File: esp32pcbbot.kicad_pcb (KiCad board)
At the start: 2 copper layers, 110 x 170 mm, 44 parts, among them IC1 BMI055, J1 TB002-500-02BE, J2 TB002-500-02BE, J3 TB002-500-02BE, J4 215299-4, J5 SSQ-120-01-L-D, J6 215299-4, Q1 2N7002, Q2 2N7002, Q3 Q_Photo_NPN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

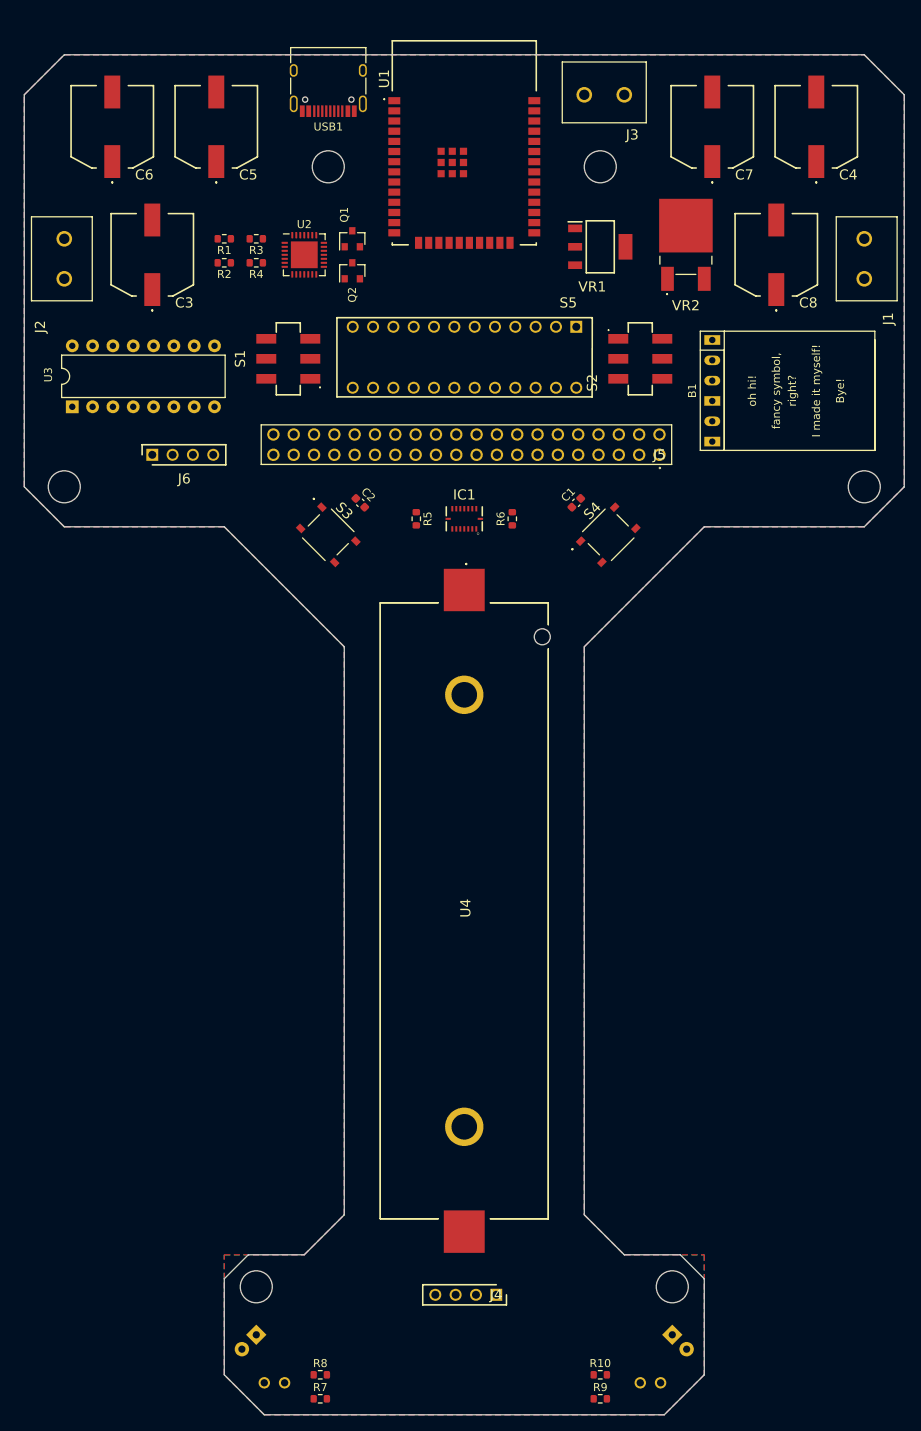
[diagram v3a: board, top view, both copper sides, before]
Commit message: rearranged AGAIN for auto routing
wow this is getting really annoying. I hope it works this time.
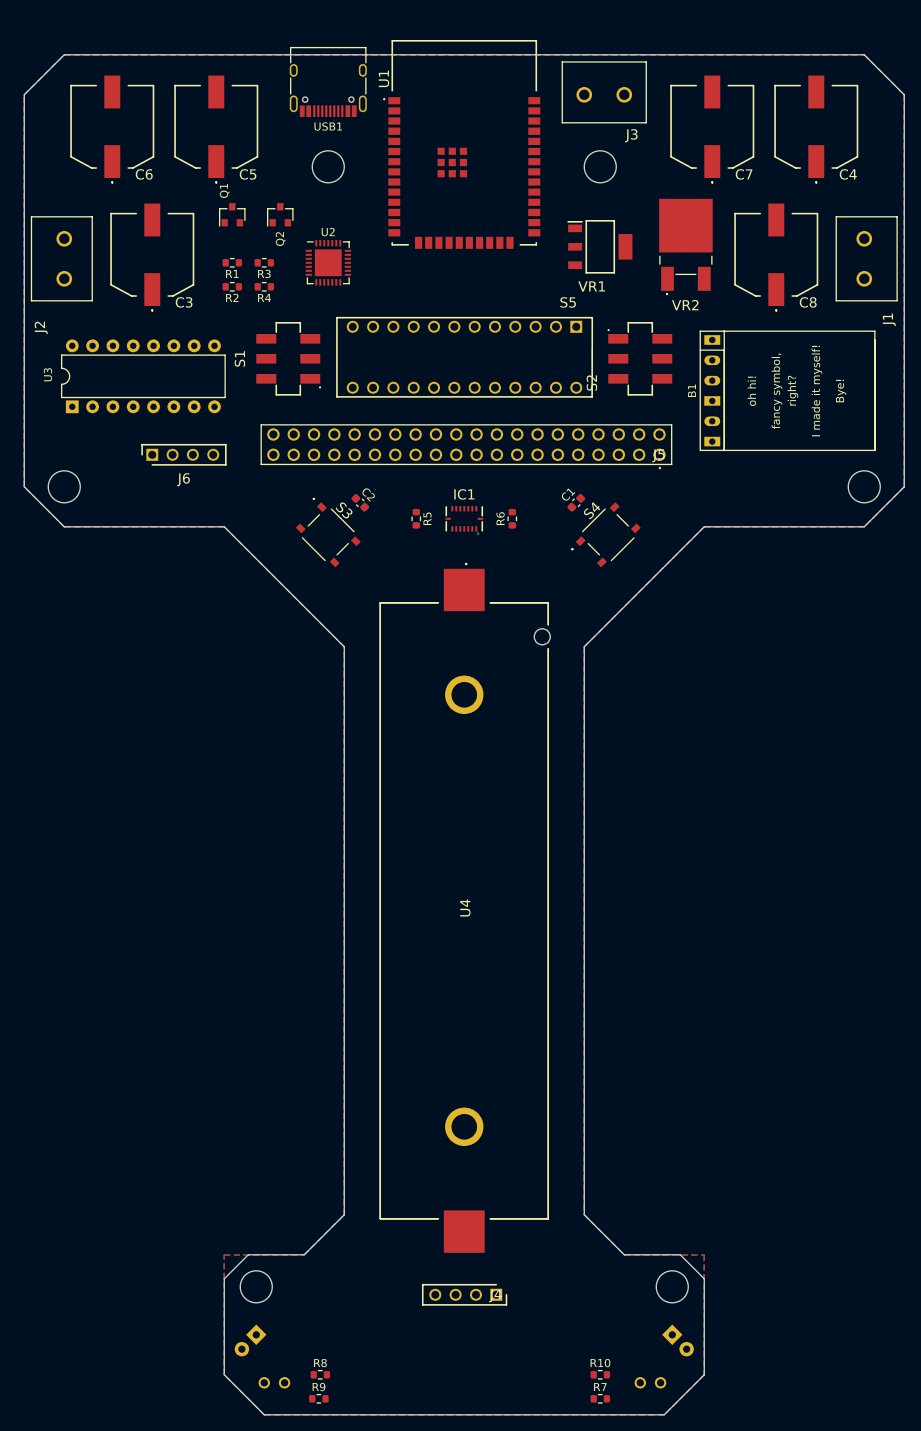
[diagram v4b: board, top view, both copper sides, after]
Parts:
- moved R9 35.2 mm to (71.8, 193.0)
- moved R7 35.0 mm to (107.0, 193.0)
- moved Q1 15.3 mm to (61.0, 45.0)
- moved Q2 11.4 mm to (67.0, 45.0)
- moved R1 3.16 mm to (61.0, 51.0)
- moved R2 3.16 mm to (61.0, 54.0)
- moved R3 3.16 mm to (65.0, 51.0)
- moved R4 3.16 mm to (65.0, 54.0)
- moved U2 3.16 mm to (73.0, 51.0)
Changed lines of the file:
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@@
   )
   (module Package_DFN_QFN:QFN-28-1EP_5x5mm_P0.5mm_EP3.35x3.35mm (layer F.Cu)
-    (at 70 50)
+    (at 73 51)
     (descr "QFN, 28 Pin (http://ww1.microchip.com/downloads/en/PackagingSpec/00000049BQ.pdf#page=283), generated with kicad-footprint-generator ipc_noLead_generator.py")
     (tags "QFN NoLead")
@@
   )
   (module Resistor_SMD:R_0603_1608Metric (layer F.Cu)
-    (at 107 193)
+    (at 71.825 193)
     (descr "Resistor SMD 0603 (1608 Metric), square (rectangular) end terminal, IPC_7351 nominal, (Body size source: IPC-SM-782 page 72, https://www.pcb-3d.com/wordpress/wp-content/uploads/ipc-sm-782a_amendment_1_and_2.pdf), generated with kicad-footprint-generator")
     (tags resistor)
@@
   )
   (module Resistor_SMD:R_0603_1608Metric (layer F.Cu)
-    (at 72 193)
+    (at 107 193)
     (descr "Resistor SMD 0603 (1608 Metric), square (rectangular) end terminal, IPC_7351 nominal, (Body size source: IPC-SM-782 page 72, https://www.pcb-3d.com/wordpress/wp-content/uploads/ipc-sm-782a_amendment_1_and_2.pdf), generated with kicad-footprint-generator")
     (tags resistor)
@@
   )
   (module Resistor_SMD:R_0603_1608Metric (layer F.Cu)
-    (at 64 51 180)
+    (at 65 54 180)
     (descr "Resistor SMD 0603 (1608 Metric), square (rectangular) end terminal, IPC_7351 nominal, (Body size source: IPC-SM-782 page 72, https://www.pcb-3d.com/wordpress/wp-content/uploads/ipc-sm-782a_amendment_1_and_2.pdf), generated with kicad-footprint-generator")
     (tags resistor)
@@
   )
   (module Resistor_SMD:R_0603_1608Metric (layer F.Cu)
-    (at 64 48 180)
+    (at 65 51 180)
     (descr "Resistor SMD 0603 (1608 Metric), square (rectangular) end terminal, IPC_7351 nominal, (Body size source: IPC-SM-782 page 72, https://www.pcb-3d.com/wordpress/wp-content/uploads/ipc-sm-782a_amendment_1_and_2.pdf), generated with kicad-footprint-generator")
     (tags resistor)
@@
   )
   (module Resistor_SMD:R_0603_1608Metric (layer F.Cu)
-    (at 60 51 180)
+    (at 61 54 180)
     (descr "Resistor SMD 0603 (1608 Metric), square (rectangular) end terminal, IPC_7351 nominal, (Body size source: IPC-SM-782 page 72, https://www.pcb-3d.com/wordpress/wp-content/uploads/ipc-sm-782a_amendment_1_and_2.pdf), generated with kicad-footprint-generator")
     (tags resistor)
@@
   )
   (module Resistor_SMD:R_0603_1608Metric (layer F.Cu)
-    (at 60 48 180)
+    (at 61 51 180)
     (descr "Resistor SMD 0603 (1608 Metric), square (rectangular) end terminal, IPC_7351 nominal, (Body size source: IPC-SM-782 page 72, https://www.pcb-3d.com/wordpress/wp-content/uploads/ipc-sm-782a_amendment_1_and_2.pdf), generated with kicad-footprint-generator")
     (tags resistor)
@@
   )
   (module Package_TO_SOT_SMD:SOT-23 (layer F.Cu)
-    (at 76 52 90)
+    (at 67 45 90)
     (descr "SOT-23, Standard")
     (tags SOT-23)
@@
   )
   (module Package_TO_SOT_SMD:SOT-23 (layer F.Cu)
-    (at 76 48 90)
+    (at 61 45 90)
     (descr "SOT-23, Standard")
     (tags SOT-23)

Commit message: ANOTHER attempt at autorouting
ughhhhh a new layout, one less mounting hole
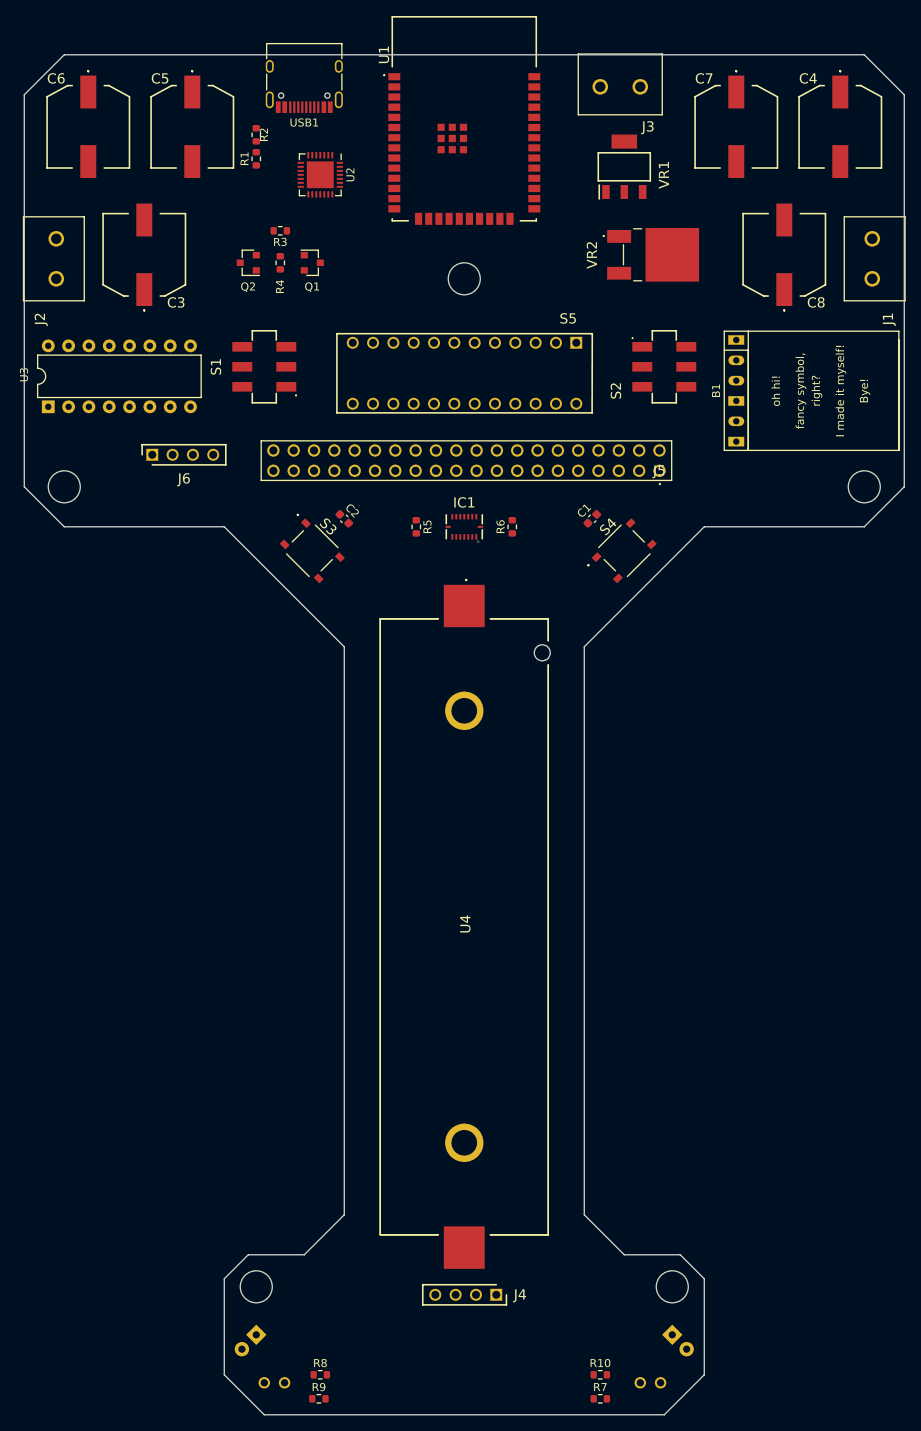
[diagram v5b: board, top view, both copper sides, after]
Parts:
- moved R2 19.2 mm to (64.0, 35.0), turned to 270 degrees
- moved R1 13.3 mm to (64.0, 38.0), turned to 90 degrees
- moved Q1 11.7 mm to (71.0, 51.0), turned to 0 degrees
- moved U2 11.0 mm to (72.0, 40.0), turned to 270 degrees
- moved VR1 10.4 mm to (110.0, 39.0), turned to 90 degrees
- moved Q2 7.21 mm to (63.0, 51.0), turned to 180 degrees
- moved VR2 5.04 mm to (112.7, 50.0), turned to 270 degrees
- moved R3 4.47 mm to (67.0, 47.0)
- moved R4 3.61 mm to (67.0, 51.0), turned to 90 degrees
- moved S1 3.16 mm to (65.0, 64.0)
- moved S2 3.16 mm to (115.0, 64.0)
- moved USB1 3.04 mm to (70.0, 27.5)
- moved B1 3.00 mm to (124.0, 67.0)
- moved C4 3.00 mm to (137.0, 34.0), turned to 180 degrees
- moved C5 3.00 mm to (56.0, 34.0), turned to 180 degrees
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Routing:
- removed copper zone on B.Cu, net GND
- removed copper zone on F.Cu, net GND
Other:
- outline, holes or cut-outs redrawn
- net class Power: trace_width 0.4 -> 0.5

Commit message: grrr more autorouting
i put the mounting holes back
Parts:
- moved C6 25.5 mm to (62.0, 51.0)
- moved C5 18.0 mm to (50.0, 51.0)
- moved C7 17.1 mm to (118.0, 50.0)
- moved C3 14.0 mm to (50.0, 36.0), turned to 180 degrees
- moved VR2 12.4 mm to (115.7, 38.0)
- moved VR1 11.4 mm to (107.0, 50.0), turned to 270 degrees
- moved Q2 10.0 mm to (71.0, 45.0), turned to 90 degrees
- moved R3 9.90 mm to (60.0, 40.0)
- moved C4 7.07 mm to (130.0, 35.0)
- moved R1 4.47 mm to (60.0, 36.0)
- moved R2 4.47 mm to (60.0, 33.0)
- moved R4 4.47 mm to (71.0, 49.0), turned to 0 degrees
- moved U2 4.47 mm to (68.0, 38.0)
- moved Q1 2.00 mm to (71.0, 53.0), turned to 270 degrees
- turned C8 to 180 degrees
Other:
- outline, holes or cut-outs redrawn

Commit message: 1 more routing
THIS IS THE LAST ONE I SWEAR IF I HAVE TO DO 1 MORE ROUTING I AM MAKING ALL 20 ROBOTS ON STRIP BOARD
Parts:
- moved Q1 17.7 mm to (59.0, 40.0)
- moved R4 17.7 mm to (59.0, 36.0)
- moved Q2 8.60 mm to (64.0, 40.0), turned to 270 degrees
- moved U2 6.08 mm to (74.0, 39.0)
- moved R3 5.66 mm to (64.0, 36.0)
- moved R1 5.39 mm to (62.0, 31.0)
- moved R2 5.39 mm to (62.0, 28.0)
- moved U1 2.00 mm to (90.0, 35.0)
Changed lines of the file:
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@@
   )
   (module Package_DFN_QFN:QFN-28-1EP_5x5mm_P0.5mm_EP3.35x3.35mm (layer F.Cu)
-    (at 68 38 270)
+    (at 74 39 270)
     (descr "QFN, 28 Pin (http://ww1.microchip.com/downloads/en/PackagingSpec/00000049BQ.pdf#page=283), generated with kicad-footprint-generator ipc_noLead_generator.py")
     (tags "QFN NoLead")
@@
   )
   (module SamacSys_Parts:ESP32WROOM32EM113EH3200PS3Q0 (layer F.Cu)
-    (at 90 33)
+    (at 90 35)
     (descr "ESP32-WROOM-32E(M113EH3200PS3Q0)-1")
     (tags "Integrated Circuit")
@@
   )
   (module Resistor_SMD:R_0603_1608Metric (layer F.Cu)
-    (at 71 49)
+    (at 59 36)
     (descr "Resistor SMD 0603 (1608 Metric), square (rectangular) end terminal, IPC_7351 nominal, (Body size source: IPC-SM-782 page 72, https://www.pcb-3d.com/wordpress/wp-content/uploads/ipc-sm-782a_amendment_1_and_2.pdf), generated with kicad-footprint-generator")
     (tags resistor)
@@
   )
   (module Resistor_SMD:R_0603_1608Metric (layer F.Cu)
-    (at 60 40 180)
-    (descr "Resistor SMD 0603 (1608 Metric), square (rectangular) end terminal, IPC_7351 nominal, (Body size source: IPC-SM-782 page 72, https://www.pcb-3d.com/wordpress/wp-content/uploads/ipc-sm-782a_amendment_1_and_2.pdf), generated with kicad-footprint-generator")
-    (tags resistor)
-    (attr smd)
-    (fp_text reference R3 (at 0 -1.43) (layer F.SilkS)
+    (at 64 36 180)
+    (descr "Resistor SMD 0603 (1608 Metric), square (rectangular) end terminal, IPC_7351 nominal, (Body size source: IPC-SM-782 page 72, https://www.pcb-3d.com/wordpress/wp-content/uploads/ipc-sm-782a_amendment_1_and_2.pdf), generated with kicad-footprint-generator")
+    (tags resistor)
+    (attr smd)
+    (fp_text reference R3 (at -3 0) (layer F.SilkS)
       (effects (font (size 1 1) (thickness 0.15)))
     )
@@
   )
   (module Resistor_SMD:R_0603_1608Metric (layer F.Cu)
-    (at 60 33 270)
+    (at 62 28 270)
     (descr "Resistor SMD 0603 (1608 Metric), square (rectangular) end terminal, IPC_7351 nominal, (Body size source: IPC-SM-782 page 72, https://www.pcb-3d.com/wordpress/wp-content/uploads/ipc-sm-782a_amendment_1_and_2.pdf), generated with kicad-footprint-generator")
     (tags resistor)
@@
   )
   (module Resistor_SMD:R_0603_1608Metric (layer F.Cu)
-    (at 60 36 90)
+    (at 62 31 90)
     (descr "Resistor SMD 0603 (1608 Metric), square (rectangular) end terminal, IPC_7351 nominal, (Body size source: IPC-SM-782 page 72, https://www.pcb-3d.com/wordpress/wp-content/uploads/ipc-sm-782a_amendment_1_and_2.pdf), generated with kicad-footprint-generator")
     (tags resistor)
@@
   )
   (module Package_TO_SOT_SMD:SOT-23 (layer F.Cu)
-    (at 71 45 90)
+    (at 64 40 270)
     (descr "SOT-23, Standard")
     (tags SOT-23)
@@
     (fp_line (start 0.76 -1.58) (end -1.4 -1.58) (layer F.SilkS) (width 0.12))
     (fp_line (start 0.76 1.58) (end -0.7 1.58) (layer F.SilkS) (width 0.12))
-    (fp_text user %R (at 0 0 270) (layer F.Fab)
+    (fp_text user %R (at 1 0 270) (layer F.Fab)
       (effects (font (size 0.5 0.5) (thickness 0.075)))
     )
-    (pad 3 smd rect (at 1 0 90) (size 0.9 0.8) (layers F.Cu F.Paste F.Mask)
+    (pad 3 smd rect (at 1 0 270) (size 0.9 0.8) (layers F.Cu F.Paste F.Mask)
       (net 5 EN))
-    (pad 2 smd rect (at -1 0.95 90) (size 0.9 0.8) (layers F.Cu F.Paste F.Mask)
+    (pad 2 smd rect (at -1 0.95 270) (size 0.9 0.8) (layers F.Cu F.Paste F.Mask)
       (net 53 "Net-(Q2-Pad2)"))
-    (pad 1 smd rect (at -1 -0.95 90) (size 0.9 0.8) (layers F.Cu F.Paste F.Mask)
+    (pad 1 smd rect (at -1 -0.95 270) (size 0.9 0.8) (layers F.Cu F.Paste F.Mask)
       (net 54 "Net-(Q2-Pad1)"))
     (model ${KISYS3DMOD}/Package_TO_SOT_SMD.3dshapes/SOT-23.wrl
@@
   )
   (module Package_TO_SOT_SMD:SOT-23 (layer F.Cu)
-    (at 71 53 270)
+    (at 59 40 270)
     (descr "SOT-23, Standard")
     (tags SOT-23)
@@
     (fp_line (start 0.76 -1.58) (end -1.4 -1.58) (layer F.SilkS) (width 0.12))
     (fp_line (start 0.76 1.58) (end -0.7 1.58) (layer F.SilkS) (width 0.12))
-    (fp_text user %R (at 0 0) (layer F.Fab)
+    (fp_text user %R (at 0 1) (layer F.Fab)
       (effects (font (size 0.5 0.5) (thickness 0.075)))
     )

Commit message: IT IS FINISHED!!!!
I THINK MY DESIGN IS FINALLY FULLY COMPLETE FUNCTIONALLY, logo and aesthetics to be added.
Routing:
- net GND: track 0.00 -> 593.8 mm, vias 0 -> 1
- net +5V: track 0.00 -> 347.6 mm, vias 0 -> 2
- net +3V3: track 0.00 -> 214.9 mm, vias 0 -> 5
- net 10Y: track 0.00 -> 173.0 mm, vias 0 -> 1
- net 12Y: track 0.00 -> 150.6 mm, vias 0 -> 2
- net 11Y: track 0.00 -> 142.3 mm
- net BOOT: track 0.00 -> 137.3 mm, vias 0 -> 2
- net VBUS: track 0.00 -> 134.7 mm, vias 0 -> 4
- net 7A: track 0.00 -> 124.9 mm, vias 0 -> 3
- net EN: track 0.00 -> 124.5 mm, vias 0 -> 3
- net 9Y: track 0.00 -> 113.6 mm
- net M1A: track 0.00 -> 107.6 mm
- net Net-(S2-Pad2): track 0.00 -> 106.6 mm, vias 0 -> 1
- net Net-(J5-Pad15): track 0.00 -> 103.4 mm, vias 0 -> 2
- net 10A: track 0.00 -> 98.5 mm, vias 0 -> 5
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- added copper zone on B.Cu, net GND
- added copper zone on F.Cu, net GND
